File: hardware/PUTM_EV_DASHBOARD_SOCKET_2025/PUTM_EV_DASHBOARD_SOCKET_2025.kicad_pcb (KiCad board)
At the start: 2 copper layers, 175.1 x 98.9 mm, 58 parts, among them J1 Conn_01x02_Pin, J1pin200000 Conn_02x20_Top_Bottom_Mountin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, J2 Conn_01x02_Pin, J2SO2 Conn_02x20_Top_Bottom_Mountin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, J3 Conn_01x02_Pin, J4 Conn_01x01, J5 Conn_01x01, J5POWER1 Conn_01x06_MountingPin, J7 FTSH, J8 Conn_01x03_Socket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

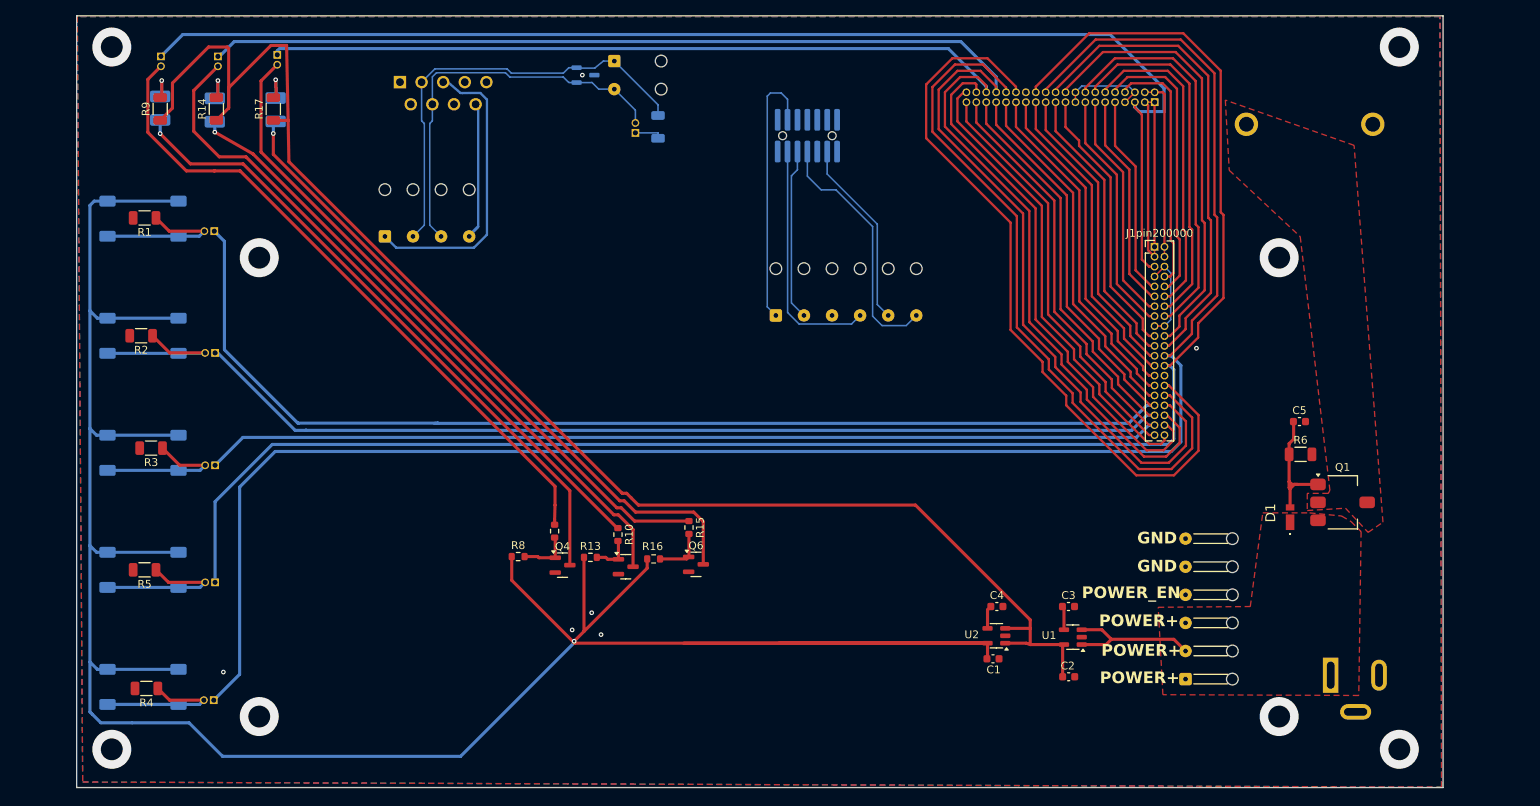
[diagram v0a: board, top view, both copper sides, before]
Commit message: fixed button logic, holes for inserts, distance from mounting holes to P4 socket, changed jumpers, TVS diode and footprint for laboratory socket 4m
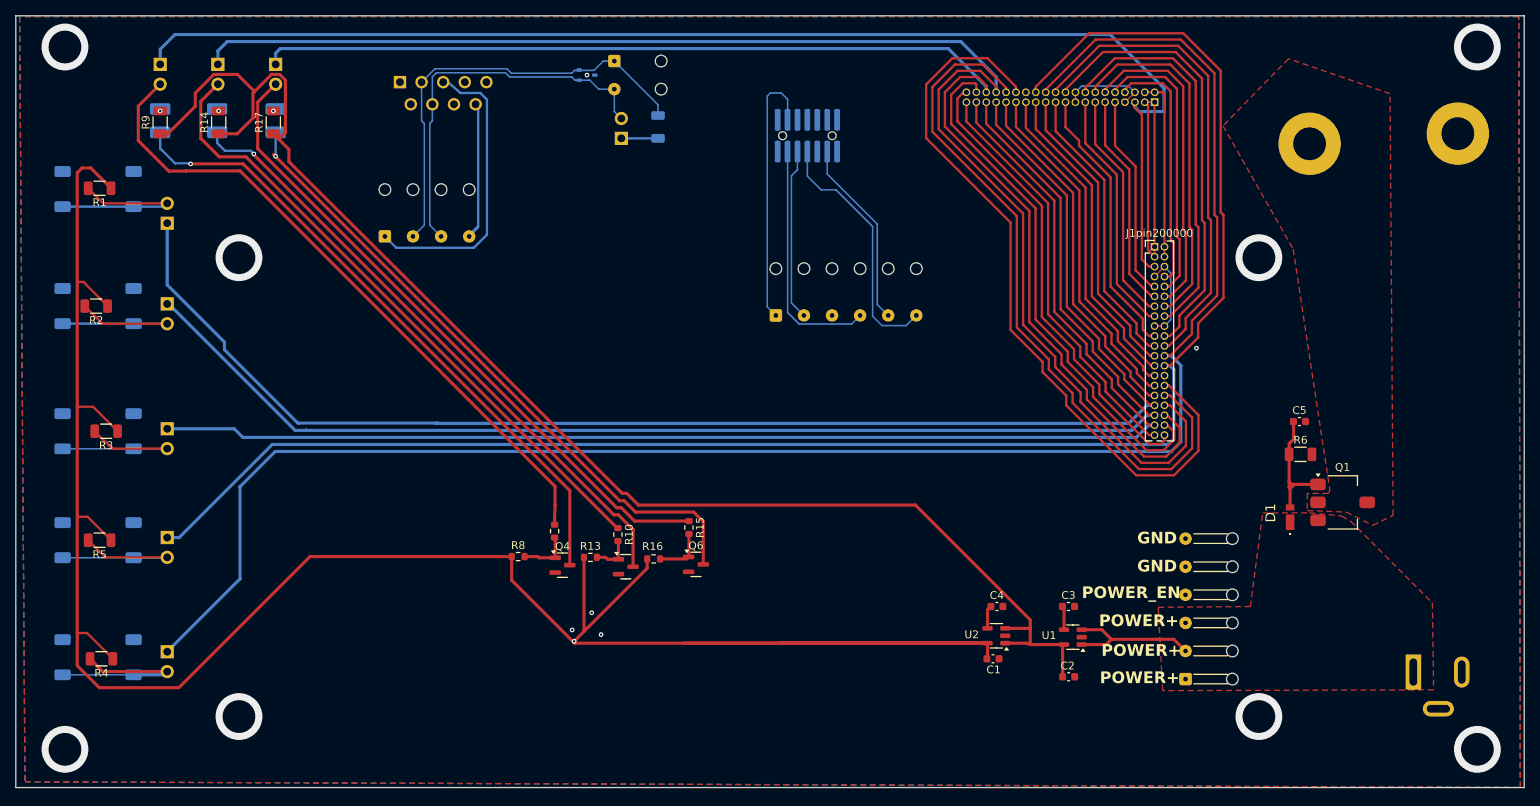
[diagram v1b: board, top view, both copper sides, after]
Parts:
- removed D8: PESD2CAN.215, Package_TO_SOT_SMD:SOT-23-3
- added D24: PESD2IVN24-U, Package_TO_SOT_SMD:SOT-323_SC-70, B.Cu at (150.9, 33.6)
- CS_BTN1, DRS_BTN1, J1, J2, J3, RTD_BTN1, TERM_1, TSA_BTN1, USR_BTN1: footprint Connector_PinHeader_1.27mm:PinHeader_1x02_P1.27mm_Vertical -> Connector_PinHeader_2.54mm:PinHeader_1x02_P2.54mm_Vertical
- J4, J5: footprint footprints:PJ3253 -> footprints:D-3230
- moved J5 11.0 mm to (262.5, 43.6)
- moved J8 10.6 mm to (256.8, 110.1)
- moved RTD_BTN1 8.78 mm to (97.1, 62.9), turned to 180 degrees
- moved USR_BTN1 8.61 mm to (97.1, 107.5), turned to 180 degrees
- moved J4 8.48 mm to (243.5, 44.9)
- moved DRS_BTN1 8.40 mm to (97.1, 92.9), turned to 180 degrees
- moved TSA_BTN1 7.71 mm to (97.1, 78.9), turned to 180 degrees
- moved R1 6.90 mm to (88.4, 48.1)
- moved R2 6.90 mm to (88.0, 63.2)
- moved R4 6.90 mm to (88.7, 108.4)
- moved R5 6.90 mm to (88.4, 93.2)
- moved SW1 6.90 mm to (88.2, 48.2)
- moved SW2 6.90 mm to (88.2, 63.2)
- moved SW4 6.90 mm to (88.2, 108.2)
- moved SW5 6.90 mm to (88.2, 93.2)
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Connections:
- R1 pad 1: /BUTTON_1 -> +3.3V
- R1 pad 2: GND -> /BUTTON_1
- R2 pad 1: /BUTTON_2 -> +3.3V
- R2 pad 2: GND -> /BUTTON_2
- R3 pad 1: /BUTTON_3 -> +3.3V
- R3 pad 2: GND -> /BUTTON_3
- R4 pad 1: /BUTTON_4 -> +3.3V
- R4 pad 2: GND -> /BUTTON_4
- R5 pad 1: /BUTTON_5 -> +3.3V
- R5 pad 2: GND -> /BUTTON_5
- SW1 pad 1: +3.3V -> GND
- SW2 pad 1: +3.3V -> GND
- SW3 pad 1: +3.3V -> GND
- SW4 pad 1: +3.3V -> GND
- SW5 pad 1: +3.3V -> GND
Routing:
- net +3.3V: track 353.2 -> 314.8 mm
- net +5V: track 191.5 -> 180.7 mm
- net /SOCKETS_2X20/P14: track 174.8 -> 183.5 mm
- net /SOCKETS_2X20/PA15: track 173.8 -> 178.9 mm
- net Net-(FUSE_LED0-A): track 4.99 -> 0.00 mm
- net /BUTTON_1: track 19.6 -> 24.5 mm
- net /BUTTON_2: track 20.2 -> 24.9 mm
- net /BUTTON_5: track 19.7 -> 24.5 mm
- net Net-(SAFETY_LED0-A): track 4.53 -> 0.00 mm
- net /BUTTON_3: track 19.2 -> 23.6 mm
- net Net-(AMS0-A): track 4.38 -> 0.00 mm
- net /BUTTON_4: track 28.2 -> 24.1 mm
- net /SOCKETS_2X20/PH11: track 230.1 -> 226.4 mm
- net /SOCKETS_2X20/PB0: track 187.8 -> 191.3 mm
- net /LED_3: track 85.0 -> 82.0 mm
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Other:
- board size 175.1 x 98.9 mm -> 193.3 x 98.9 mm

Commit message: fixed layout
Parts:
- removed SW1, SW2, SW3, SW4, SW5: SW_Push, Button_Switch_SMD:SW_Push_1P1T_NO_E-Switch_TL3301NxxxxxG
- added G***: LOGO, LOGO, F.Cu at (172.0, 86.8)
- added S1: PTS526SM15SMTR2_LFS, SamacSys_Parts:PTS526SM15SMTR2LFS, B.Cu at (87.2, 50.4)
- added S2: PTS526SM15SMTR2_LFS, SamacSys_Parts:PTS526SM15SMTR2LFS, B.Cu at (86.9, 65.9)
- added S3: PTS526SM15SMTR2_LFS, SamacSys_Parts:PTS526SM15SMTR2LFS, B.Cu at (86.9, 110.2)
- added S4: PTS526SM15SMTR2_LFS, SamacSys_Parts:PTS526SM15SMTR2LFS, B.Cu at (87.0, 81.8)
- added S5: PTS526SM15SMTR2_LFS, SamacSys_Parts:PTS526SM15SMTR2LFS, B.Cu at (86.9, 96.0)
- moved R3 3.24 mm to (87.0, 81.5), turned to 0 degrees
- moved R5 2.63 mm to (87.0, 95.4), turned to 0 degrees
- moved R2 2.50 mm to (86.9, 65.5), turned to 0 degrees
- moved R4 2.32 mm to (87.0, 110.0), turned to 0 degrees
- moved R1 2.08 mm to (87.6, 50.0), turned to 0 degrees
- moved J5 1.49 mm to (262.0, 45.0)
- moved J4 0.10 mm to (243.5, 45.0)
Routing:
- net +3.3V: track 314.8 -> 303.7 mm
- net /BUTTON_1: track 24.5 -> 21.8 mm
- net /BUTTON_2: track 24.9 -> 23.0 mm
- net /BUTTON_5: track 24.5 -> 22.8 mm
- net /BUTTON_4: track 24.1 -> 23.0 mm
- net /BUTTON_3: track 23.6 -> 22.9 mm

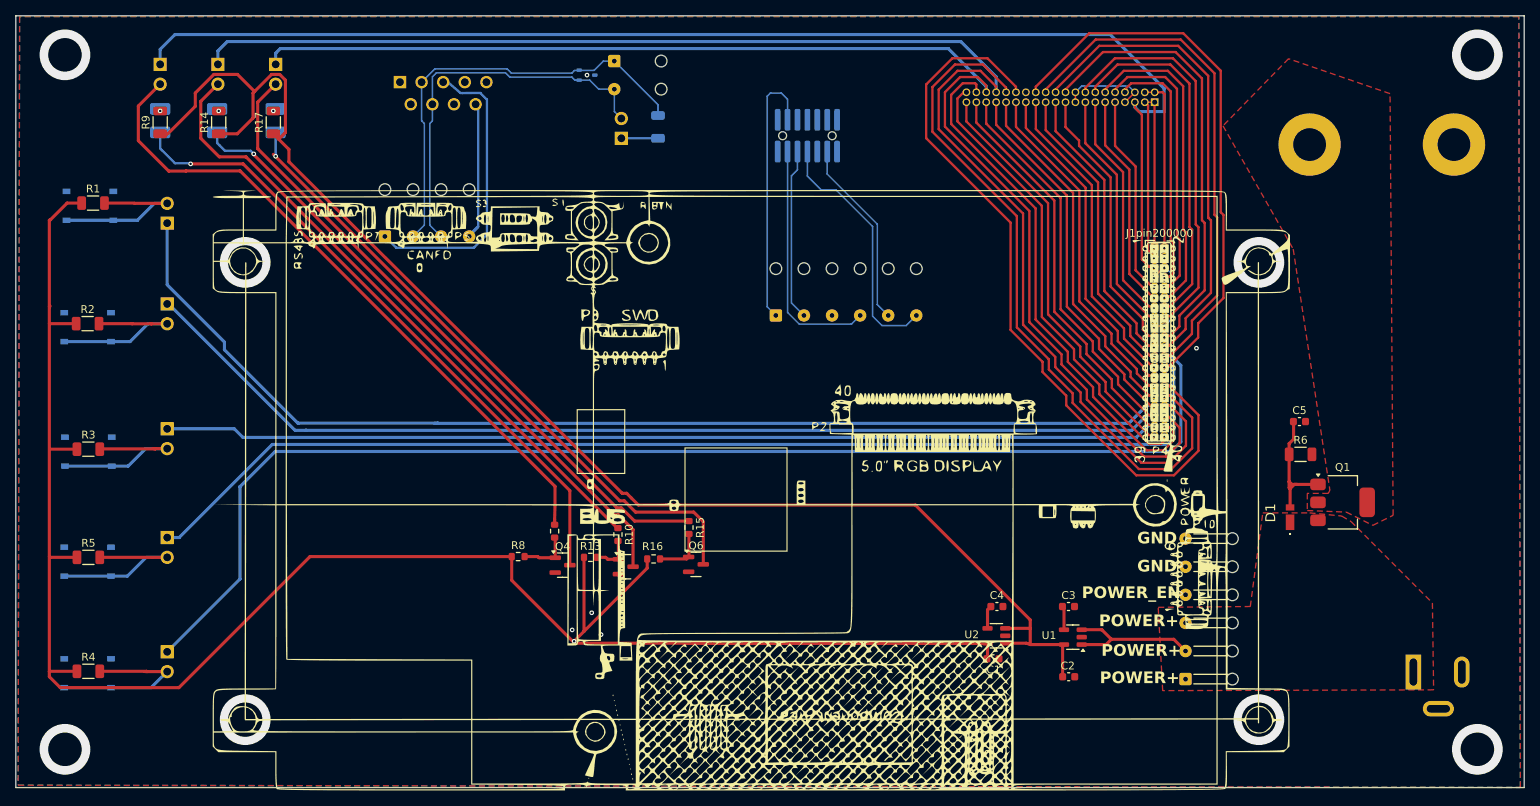
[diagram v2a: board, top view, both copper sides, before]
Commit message: fixed button text layout
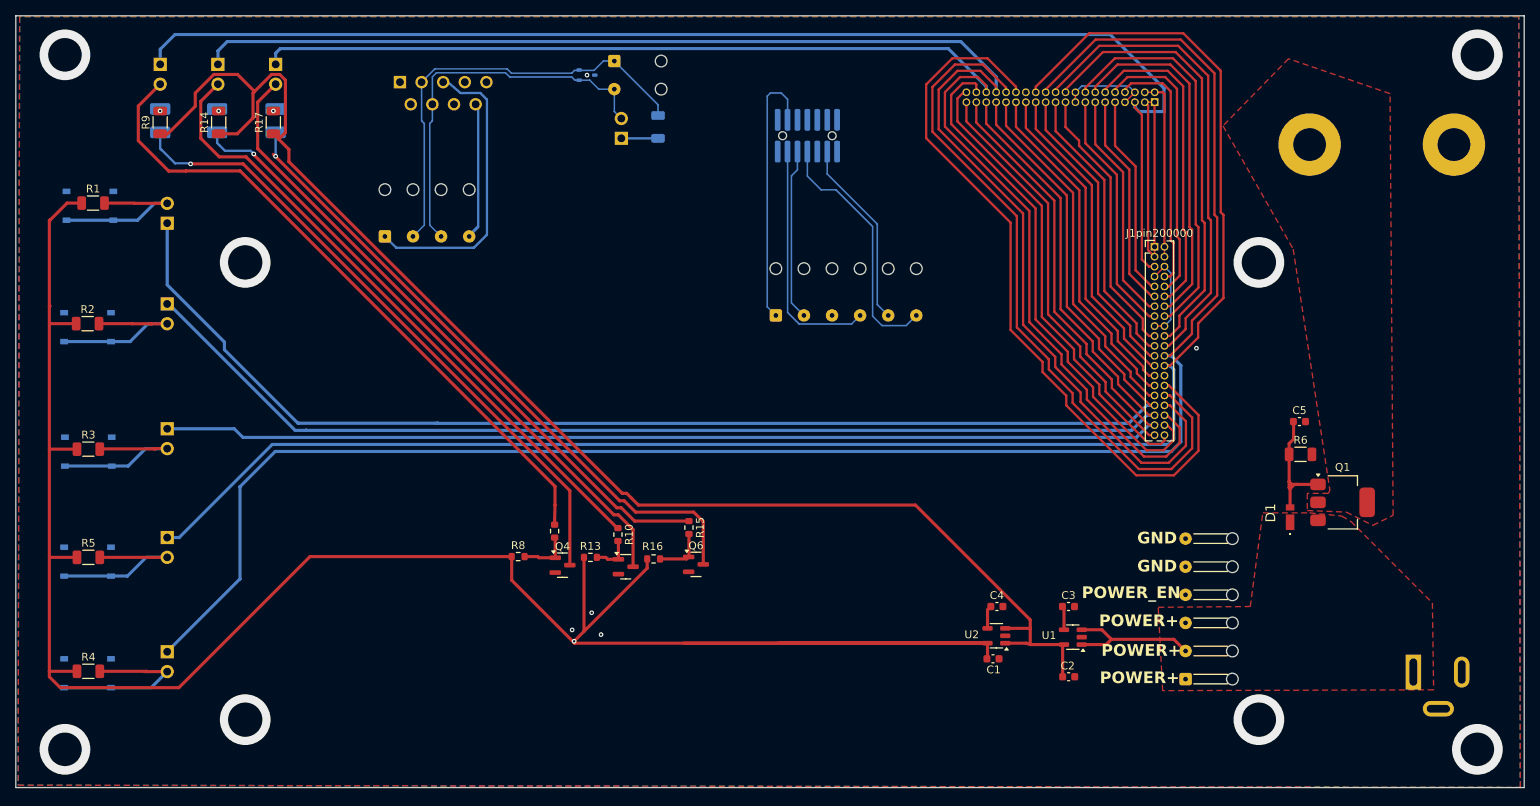
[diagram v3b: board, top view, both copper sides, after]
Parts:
- removed the G*** at (172.0, 86.8)
